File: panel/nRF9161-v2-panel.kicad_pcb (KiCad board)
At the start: 4 copper layers, 118 x 93 mm, 474 parts, among them J2 U.FL_LTE_NR+, J20 HOST_1x10_2.54, J5 U.FL_GNSS, J7 nanoSIM_4FF, J8 SWD_10pin, Q1 BSS138, SW2 RESET, U1 NRF9161-LACA-R7, U2 TLV73333PDBV, U3 TPS22919DCKR, U4 TPD3F303DPV, U5 SN74LXC2T45, U6 SN74LXC2T45, U7 SN74LXC1T45, U8 SN74LXC1T45

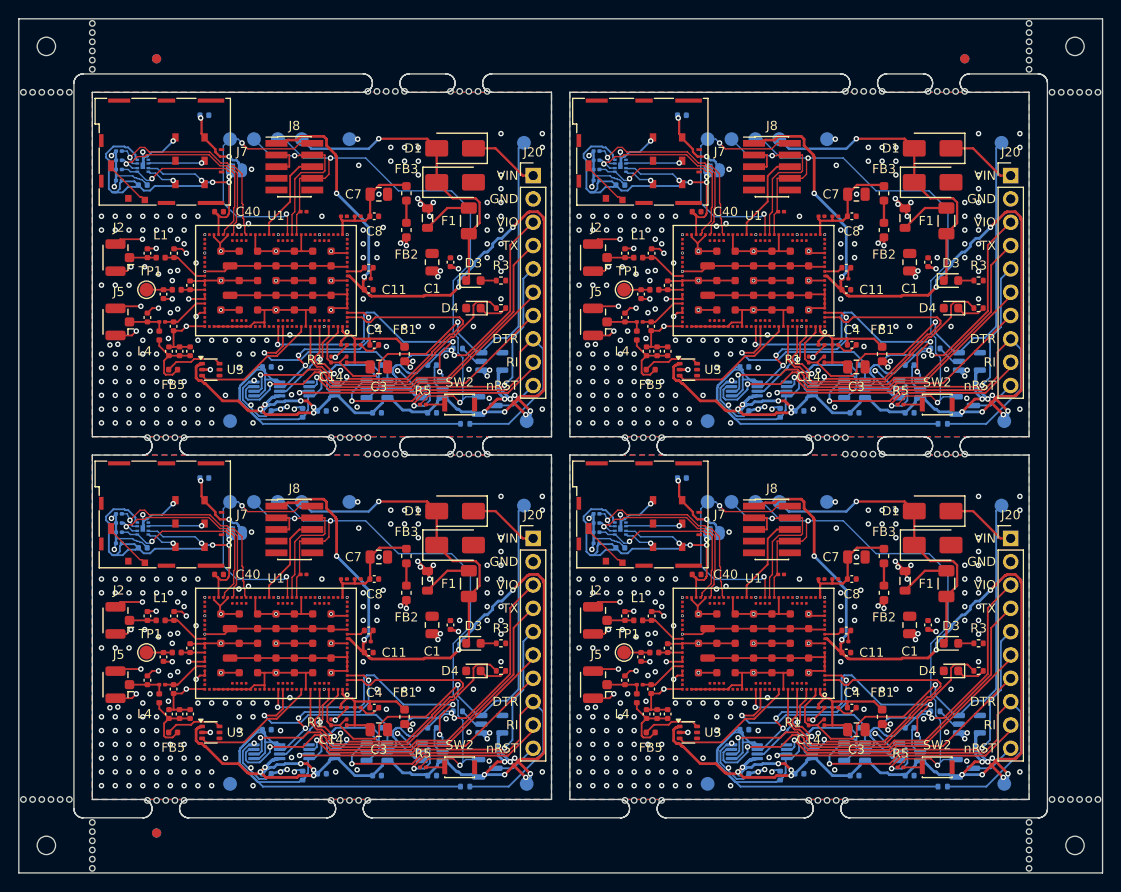
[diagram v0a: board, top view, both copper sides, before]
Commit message: v2 fab pass @d89dc88: 0.20 drill classification + option (a) recommendation (pending HW PM), regenerated panel and staging package, checklist (gate RED)
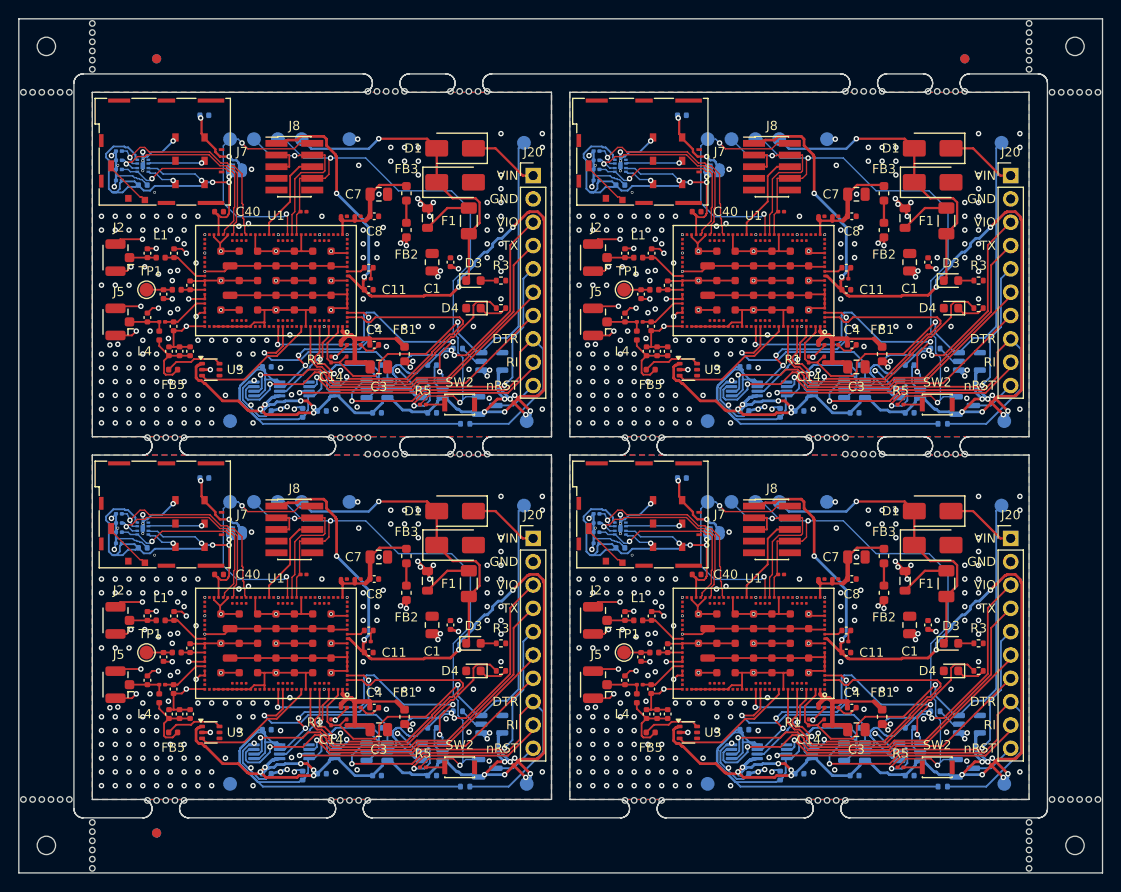
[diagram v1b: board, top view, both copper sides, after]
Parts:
- moved KiKit_MB_10_5 47.0 mm to (103.5, 105.1)
- moved KiKit_MB_11_5 47.0 mm to (131.5, 67.4)
- moved KiKit_MB_14_5 47.0 mm to (155.5, 105.1)
- moved KiKit_MB_15_5 47.0 mm to (183.5, 67.4)
- moved KiKit_MB_2_5 47.0 mm to (103.5, 65.6)
- moved KiKit_MB_3_5 47.0 mm to (131.5, 27.9)
- moved KiKit_MB_6_5 47.0 mm to (155.5, 65.6)
- moved KiKit_MB_7_5 47.0 mm to (183.5, 27.9)
- moved KiKit_MB_10_4 45.8 mm to (104.5, 105.1)
- moved KiKit_MB_11_4 45.8 mm to (130.5, 67.4)
- moved KiKit_MB_14_4 45.8 mm to (156.5, 105.1)
- moved KiKit_MB_15_4 45.8 mm to (182.5, 67.4)
- moved KiKit_MB_2_4 45.8 mm to (104.5, 65.6)
- moved KiKit_MB_3_4 45.8 mm to (130.5, 27.9)
- moved KiKit_MB_6_4 45.8 mm to (156.5, 65.6)
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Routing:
- net Board_2-GND: track 151.1 -> 152.2 mm, vias 180 -> 184
- net Board_1-GND: track 151.1 -> 152.2 mm, vias 180 -> 184
- net Board_3-GND: track 151.1 -> 152.2 mm, vias 180 -> 184
- net Board_0-GND: track 151.1 -> 152.2 mm, vias 180 -> 184

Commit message: v2 fab pass @365b7f6: fill-every-0.20 confirmed (20 vias), panel + package regenerated, checklist RED (C38.2, C12.1 via-in-pad)
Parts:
- removed the C33 at (103.0, 77.6)
- removed the C33 at (155.0, 38.1)
- removed the C33 at (103.0, 38.1)
- removed the C33 at (155.0, 77.6)
- removed the C34 at (109.7, 30.5)
- removed the C34 at (161.7, 70.0)
- removed the C34 at (109.7, 70.0)
- removed the C34 at (161.7, 30.5)
- removed the C35 at (152.4, 35.4)
- removed the C35 at (152.4, 74.9)
- removed the C35 at (100.4, 74.9)
- removed the C35 at (100.4, 35.4)
- removed the C36 at (100.4, 34.4)
- removed the C36 at (100.4, 73.9)
- removed the C36 at (152.4, 73.9)
- removed the C36 at (152.4, 34.4)
- removed the C37 at (100.4, 36.4)
- removed the C37 at (152.4, 36.4)
- removed the C37 at (100.4, 75.9)
- removed the C37 at (152.4, 75.9)
- removed the C38 at (152.4, 77.1)
- removed the C38 at (100.4, 37.6)
- removed the C38 at (152.4, 37.6)
- removed the C38 at (100.4, 77.1)
- removed the C40 at (163.3, 80.5)
- removed the C40 at (111.3, 80.5)
- removed the C40 at (163.3, 41.0)
- removed the C40 at (111.3, 41.0)
- removed the U4 at (155.0, 36.0)
- removed the U4 at (103.0, 36.0)
- removed the U4 at (155.0, 75.5)
- removed the U4 at (103.0, 75.5)
- added C33: 100nF, Capacitor_SMD:C_0402_1005Metric, F.Cu at (166.8, 38.1)
- added C33: 100nF, Capacitor_SMD:C_0402_1005Metric, F.Cu at (114.8, 38.1)
- added C33: 100nF, Capacitor_SMD:C_0402_1005Metric, F.Cu at (114.8, 77.6)
- added C33: 100nF, Capacitor_SMD:C_0402_1005Metric, F.Cu at (166.8, 77.6)
- added C34: 220nF, Capacitor_SMD:C_0402_1005Metric, F.Cu at (113.8, 33.8)
- added C34: 220nF, Capacitor_SMD:C_0402_1005Metric, F.Cu at (165.8, 33.8)
- added C34: 220nF, Capacitor_SMD:C_0402_1005Metric, F.Cu at (113.8, 73.3)
- added C34: 220nF, Capacitor_SMD:C_0402_1005Metric, F.Cu at (165.8, 73.3)
- added C35: 22pF, Capacitor_SMD:C_0201_0603Metric, F.Cu at (116.0, 80.3)
- added C35: 22pF, Capacitor_SMD:C_0201_0603Metric, F.Cu at (167.9, 40.8)
- added C35: 22pF, Capacitor_SMD:C_0201_0603Metric, F.Cu at (116.0, 40.8)
- added C35: 22pF, Capacitor_SMD:C_0201_0603Metric, F.Cu at (167.9, 80.3)
- added C36: 22pF, Capacitor_SMD:C_0201_0603Metric, F.Cu at (114.9, 42.0)
- added C36: 22pF, Capacitor_SMD:C_0201_0603Metric, F.Cu at (166.9, 42.0)
- added C36: 22pF, Capacitor_SMD:C_0201_0603Metric, F.Cu at (114.9, 81.5)
- added C36: 22pF, Capacitor_SMD:C_0201_0603Metric, F.Cu at (166.9, 81.5)
- added C37: 22pF, Capacitor_SMD:C_0201_0603Metric, F.Cu at (116.8, 80.3)
- added C37: 22pF, Capacitor_SMD:C_0201_0603Metric, F.Cu at (168.8, 80.3)
- added C37: 22pF, Capacitor_SMD:C_0201_0603Metric, F.Cu at (168.8, 40.8)
- added C37: 22pF, Capacitor_SMD:C_0201_0603Metric, F.Cu at (116.8, 40.8)
- added C38: 22pF, Capacitor_SMD:C_0201_0603Metric, F.Cu at (166.8, 75.9)
- added C38: 22pF, Capacitor_SMD:C_0201_0603Metric, F.Cu at (114.8, 36.4)
- added C38: 22pF, Capacitor_SMD:C_0201_0603Metric, F.Cu at (166.8, 36.4)
- added C38: 22pF, Capacitor_SMD:C_0201_0603Metric, F.Cu at (114.8, 75.9)
- added C40: 100nF, Capacitor_SMD:C_0402_1005Metric, F.Cu at (111.1, 80.5)
- added C40: 100nF, Capacitor_SMD:C_0402_1005Metric, F.Cu at (163.1, 41.0)
- added C40: 100nF, Capacitor_SMD:C_0402_1005Metric, F.Cu at (163.1, 80.5)
- added C40: 100nF, Capacitor_SMD:C_0402_1005Metric, F.Cu at (111.1, 41.0)
- added U4: TPD3F303DPV, Board:TI_TPD3F303_USON-8_1.45x1.45mm_P0.4mm, F.Cu at (113.9, 79.9)
- added U4: TPD3F303DPV, Board:TI_TPD3F303_USON-8_1.45x1.45mm_P0.4mm, F.Cu at (165.9, 40.4)
- added U4: TPD3F303DPV, Board:TI_TPD3F303_USON-8_1.45x1.45mm_P0.4mm, F.Cu at (113.9, 40.4)
- added U4: TPD3F303DPV, Board:TI_TPD3F303_USON-8_1.45x1.45mm_P0.4mm, F.Cu at (165.9, 79.9)
- moved KiKit_MB_12_5 52.8 mm to (103.5, 105.1)
- moved KiKit_MB_16_5 52.8 mm to (155.5, 105.1)
- moved KiKit_MB_4_5 52.8 mm to (103.5, 65.6)
- moved KiKit_MB_8_5 52.8 mm to (155.5, 65.6)
- moved KiKit_MB_12_4 51.4 mm to (104.5, 105.1)
- moved KiKit_MB_16_4 51.4 mm to (156.5, 105.1)
- moved KiKit_MB_4_4 51.4 mm to (104.5, 65.6)
- moved KiKit_MB_8_4 51.4 mm to (156.5, 65.6)
- moved KiKit_MB_12_3 50.1 mm to (105.5, 105.1)
- moved KiKit_MB_16_3 50.1 mm to (157.5, 105.1)
- moved KiKit_MB_4_3 50.1 mm to (105.5, 65.6)
- moved KiKit_MB_8_3 50.1 mm to (157.5, 65.6)
- moved KiKit_MB_4_2 48.8 mm to (106.5, 65.6)
- moved KiKit_MB_8_2 48.8 mm to (158.5, 65.6)
- moved KiKit_MB_12_2 48.8 mm to (106.5, 105.1)
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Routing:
- net Board_2-SIM_RST: track 22.9 -> 2.95 mm, vias 1 -> 0
- net Board_0-SIM_RST: track 22.9 -> 2.95 mm, vias 1 -> 0
- net Board_3-SIM_RST: track 22.9 -> 2.95 mm, vias 1 -> 0
- net Board_1-SIM_RST: track 22.9 -> 2.95 mm, vias 1 -> 0
- net Board_1-SIM_CLK: track 22.1 -> 7.25 mm, vias 1 -> 2
- net Board_3-SIM_CLK: track 22.1 -> 7.25 mm, vias 1 -> 2
- net Board_0-SIM_CLK: track 22.1 -> 7.25 mm, vias 1 -> 2
- net Board_2-SIM_CLK: track 22.1 -> 7.25 mm, vias 1 -> 2
- net Board_3-SIM_1V8: track 35.6 -> 21.9 mm, vias 3 -> 2
- net Board_1-SIM_1V8: track 35.6 -> 21.9 mm, vias 3 -> 2
- net Board_2-SIM_1V8: track 35.6 -> 21.9 mm, vias 3 -> 2
- net Board_0-SIM_1V8: track 35.6 -> 21.9 mm, vias 3 -> 2
- net Board_1-SIM_IO: track 20.5 -> 9.59 mm, vias 1 -> 2
- net Board_3-SIM_IO: track 20.5 -> 9.59 mm, vias 1 -> 2
- net Board_0-SIM_IO: track 20.5 -> 9.59 mm, vias 1 -> 2
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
